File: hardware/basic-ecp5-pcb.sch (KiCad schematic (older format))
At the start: 65 parts, among them J1 Conn_01x02, J2 Conn_02x20_Odd_Even, J3 Conn_02x06_Odd_Even, J4 Conn_02x06_Odd_Even, J5 Conn_02x06_Odd_Even, J6 Conn_02x06_Odd_Even, J7 Conn_02x06_Odd_Even, J8 Conn_02x06_Odd_Even, J9 Conn_02x20_Odd_Even, Q1 Q_NMOS_GSD, SW1 SW_Push, SW2 SW_Push, U2 IS25LP016D-JBLE, U3 TLV62568DBV, U4 TLV62568DBV, U5 TLV73325PDBV, X1 SiT2001B

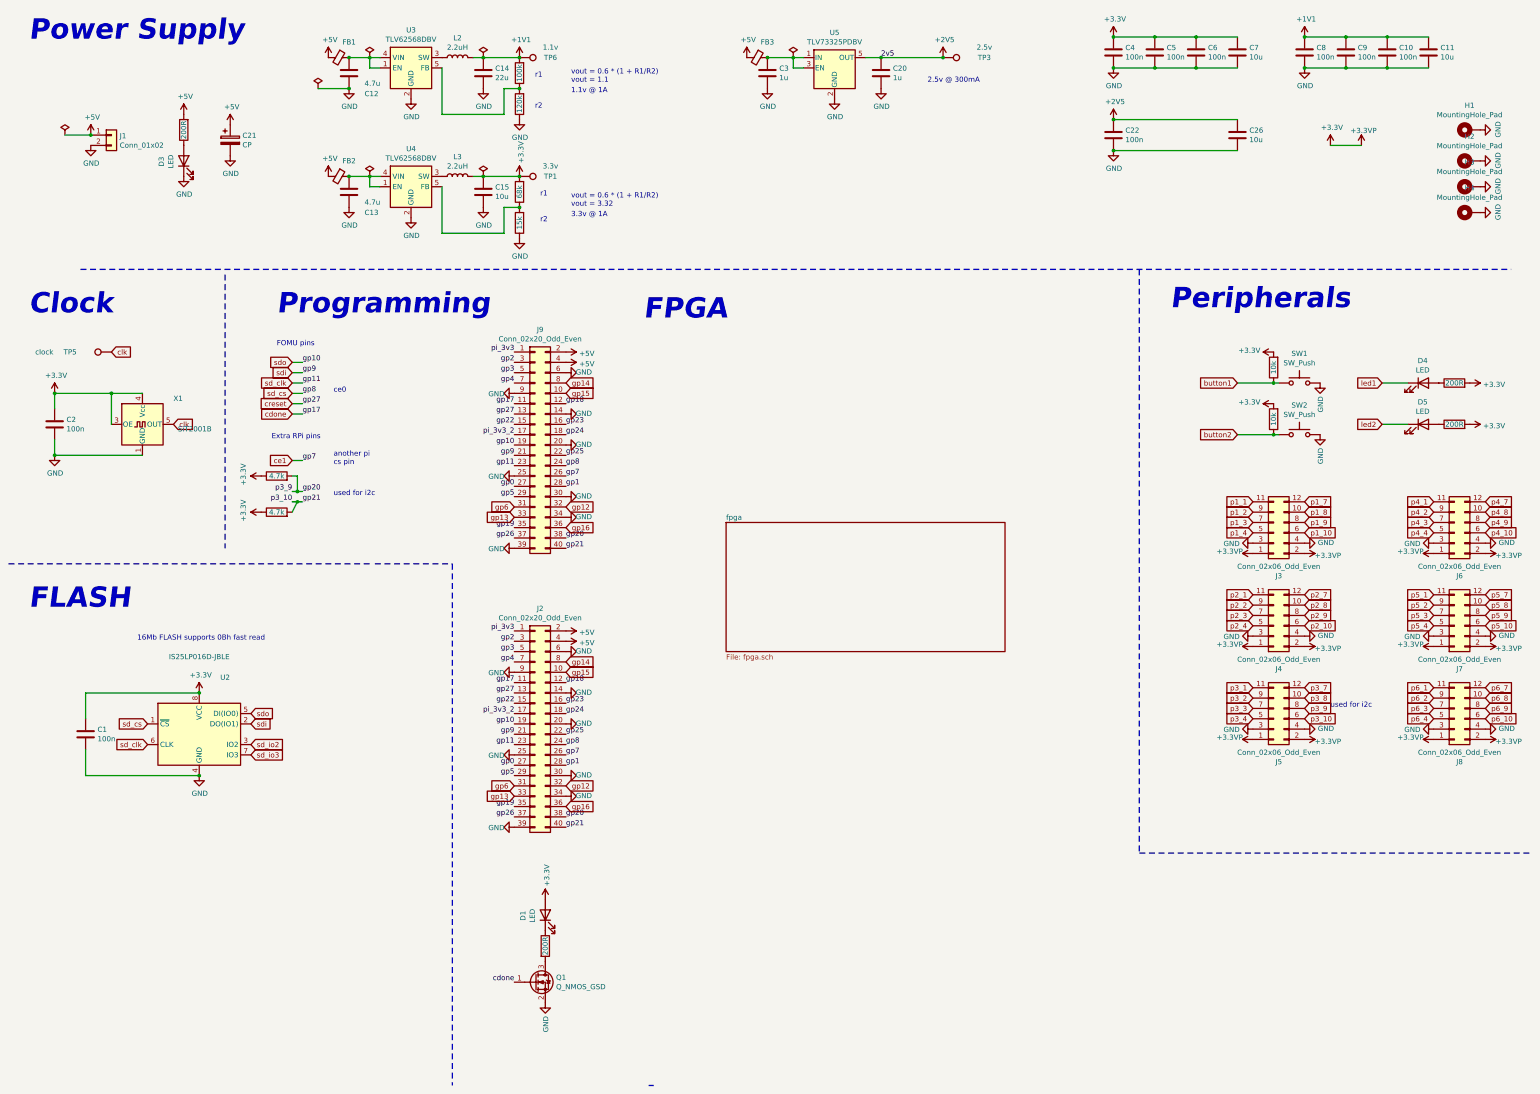
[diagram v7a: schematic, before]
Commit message: neaten FPGA page
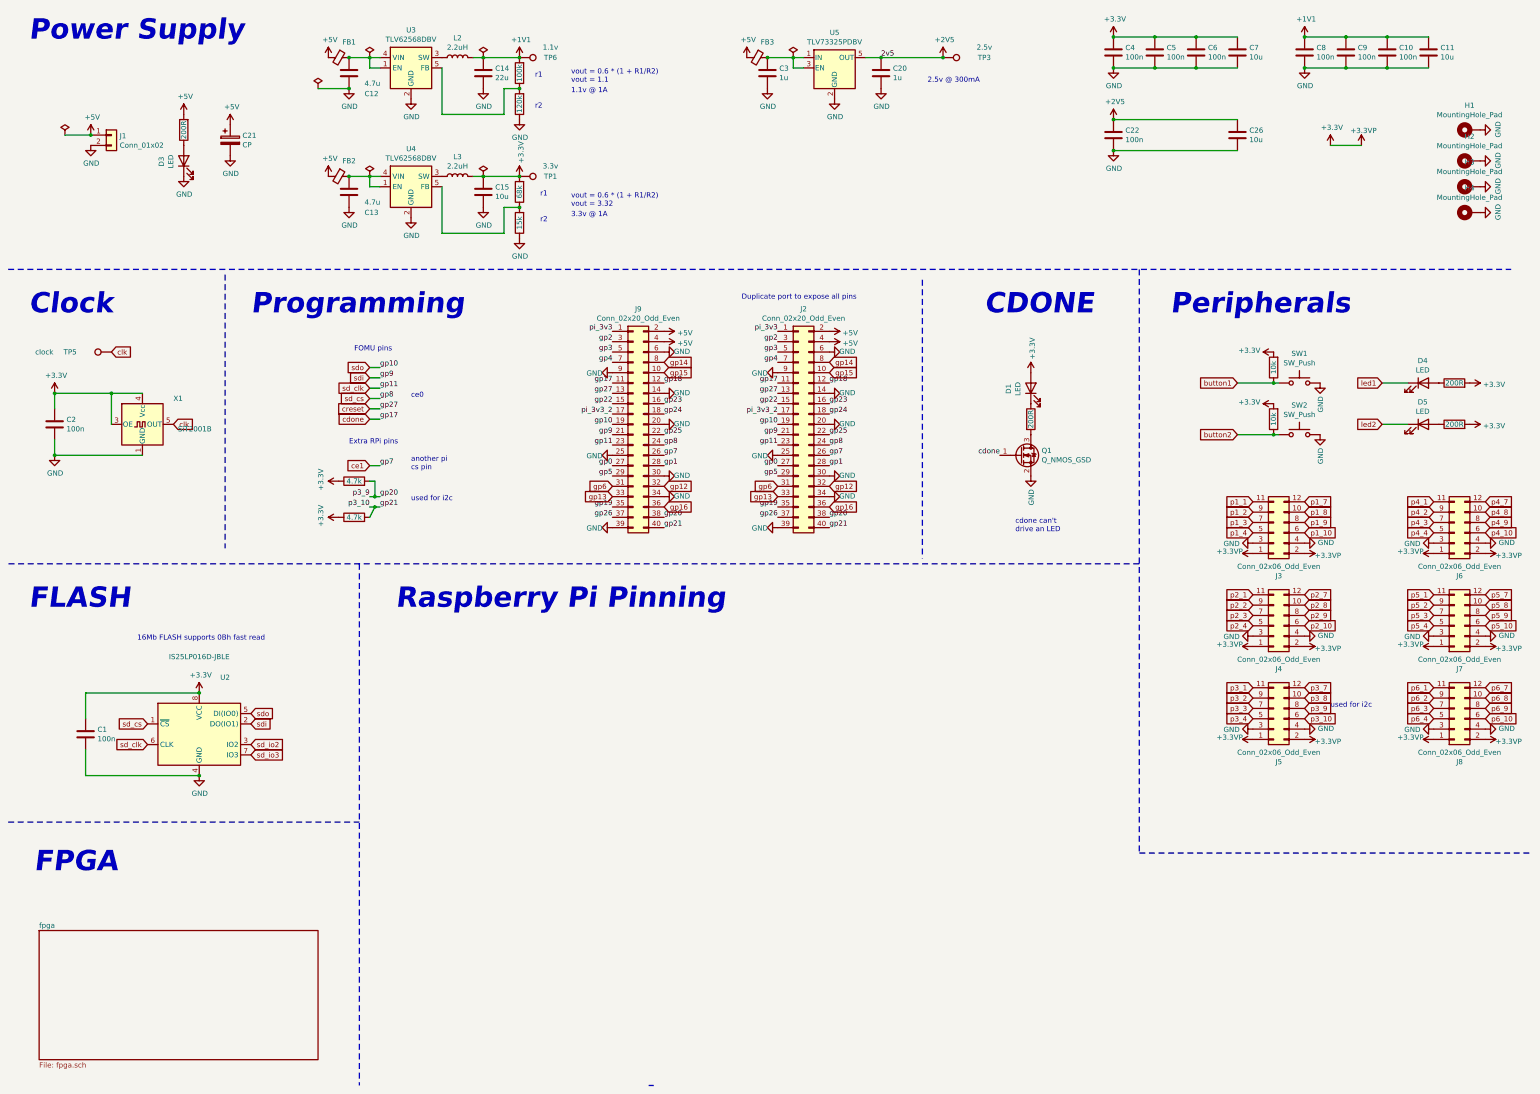
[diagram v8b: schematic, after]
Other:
- note added: "CDONE"
- note added: "Duplicate port to expose all pins"
- note added: "Raspberry Pi Pinning"
- note added: "cdone can't \ndrive an LED"
- moved on the sheet: D1, J2, J9, Q1
